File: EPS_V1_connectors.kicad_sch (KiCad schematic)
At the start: 4 parts, among them J1 Conn_01x20_Socket, J2 Conn_01x30_Socket, J3 Conn_01x15_Socket, J4 Conn_01x04_Socket

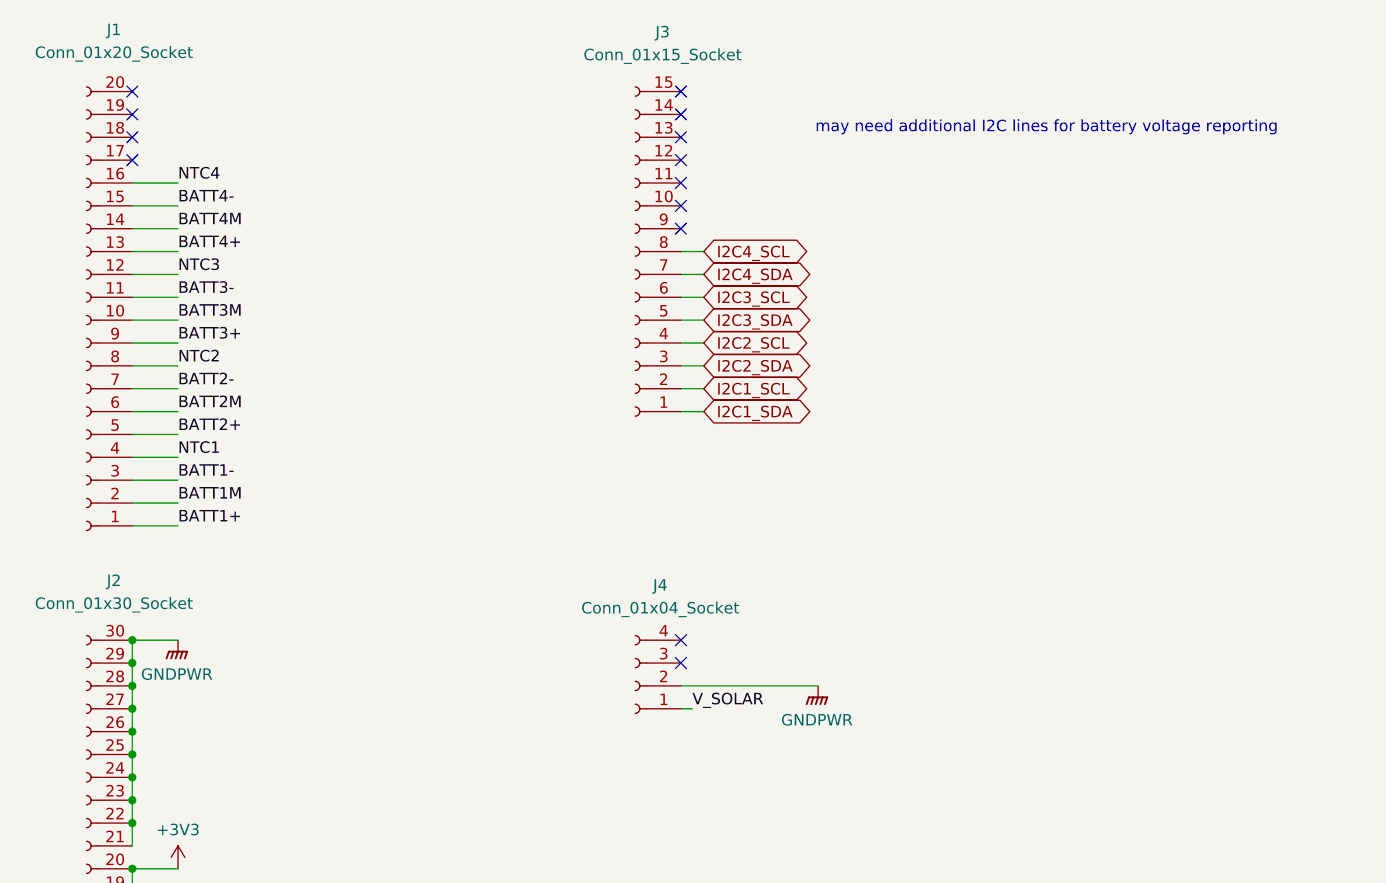
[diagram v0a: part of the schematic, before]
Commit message: Add fuel gauge, fix voltage labels
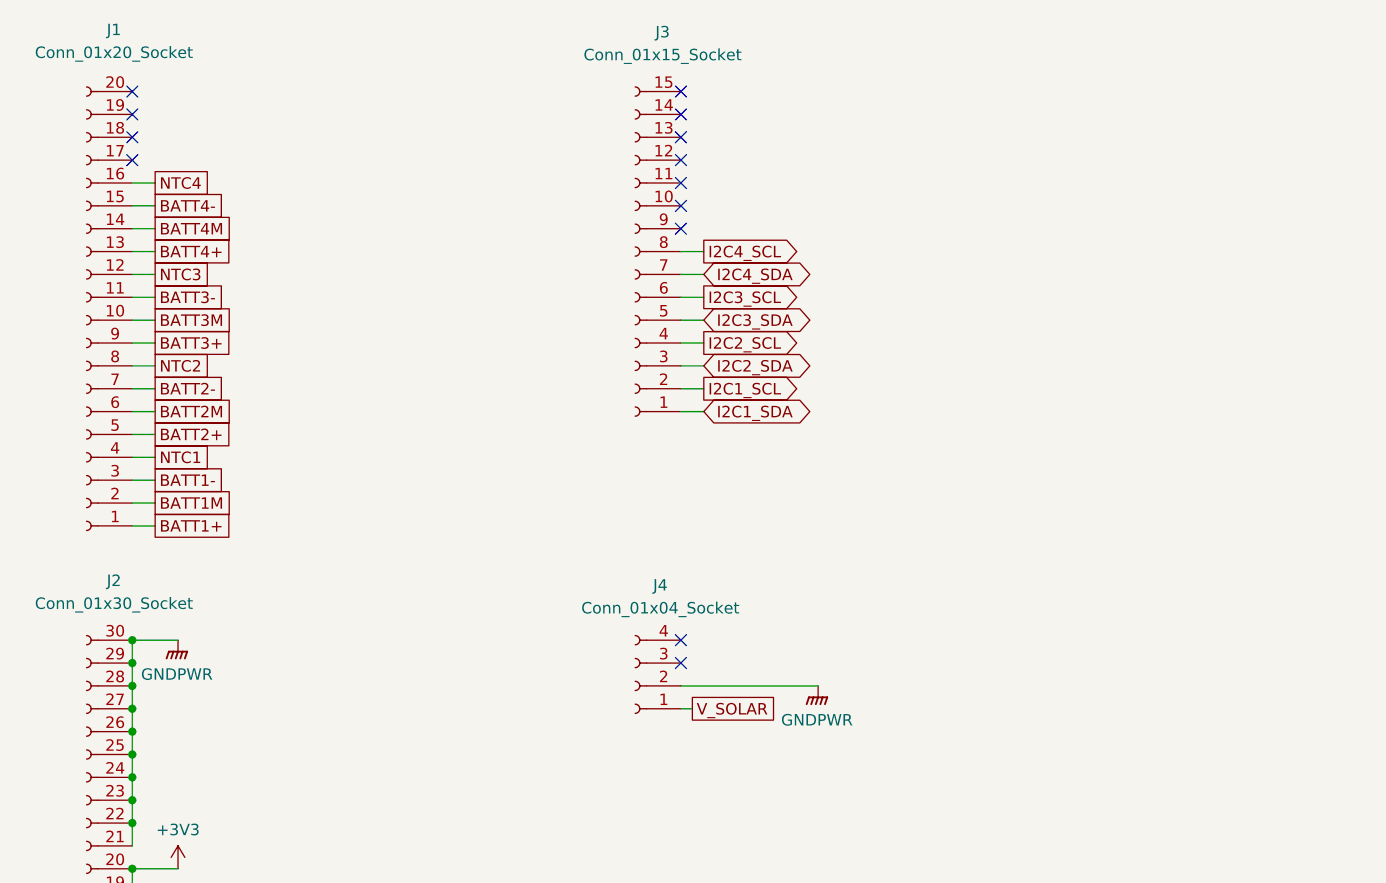
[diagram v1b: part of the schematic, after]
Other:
- note removed: "may need additional I2C lines for battery voltage reporting"

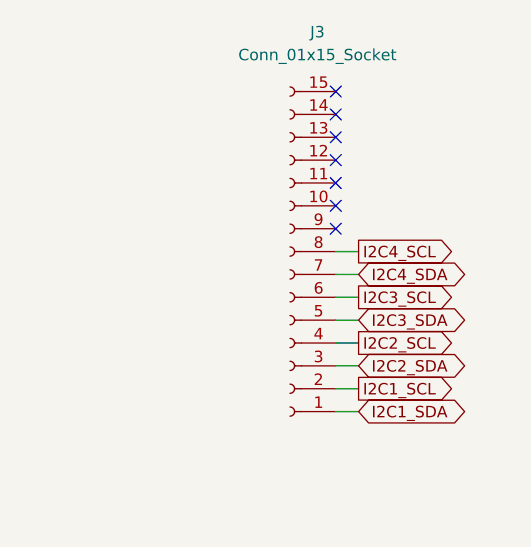
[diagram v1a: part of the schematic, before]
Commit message: Add fuel gauge ALRT lines
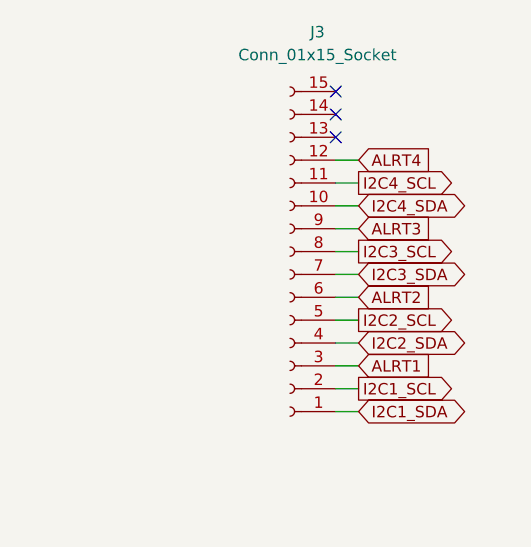
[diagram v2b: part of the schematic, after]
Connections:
- net I2C2_SCL: now also J3.5 (Pin_5); no longer J3.4 (Pin_4)
- net I2C2_SDA: now also J3.4 (Pin_4); no longer J3.3 (Pin_3)
- net I2C3_SCL: now also J3.8 (Pin_8); no longer J3.6 (Pin_6)
- net I2C3_SDA: now also J3.7 (Pin_7); no longer J3.5 (Pin_5)
- net I2C4_SCL: now also J3.11 (Pin_11); no longer J3.8 (Pin_8)
- net I2C4_SDA: now also J3.10 (Pin_10); no longer J3.7 (Pin_7)
- net ALRT4: now reaches J3.12 (Pin_12)
- net ALRT3: now reaches J3.9 (Pin_9)
- new net ALRT1: J3.3 (Pin_3)
- new net ALRT2: J3.6 (Pin_6)
- no-connect marks 13 -> 9

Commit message: Add boost converter to 12V, fix grounding
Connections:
- net +7V2 renamed +12V
- net GNDPWR renamed GND

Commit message: Add 12V boost values
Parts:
- added D1, D2, D3, D4: D_Schottky, symbol Device:D_Schottky
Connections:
- net V_SOLAR renamed VSOLAR
- new net VOUT: D1.1 (K), D2.1 (K), D3.1 (K), D4.1 (K)
- new net VOUT1: D1.2 (A)
- new net VOUT2: D2.2 (A)
- new net VOUT3: D3.2 (A)
- new net VOUT4: D4.2 (A)
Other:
- note added: "todo: add inhibit switch"
- note added: "todo: add inhibit switches"

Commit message: Add 5V charging input
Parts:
- added D5, D6: D_Schottky, symbol Device:D_Schottky
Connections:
- net GND: now also J1.18 (Pin_18)
- net VSOLAR: now also J1.17 (Pin_17); no longer J4.1 (Pin_1)
- new net VCHG: D6.2 (A), J4.1 (Pin_1)
- new net VIN: D5.1 (K), D6.1 (K)
- new net VSOLARR: D5.2 (A)
- no-connect marks 9 -> 7

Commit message: Clarify global net naming, other minor fixes
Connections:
- net VCHG renamed EXT_5V
- net VIN renamed CHG_IN
- net VOUT renamed CHG_OUT
- net VOUT1 renamed CHG_OUT1
- net VOUT2 renamed CHG_OUT2
- net VOUT3 renamed CHG_OUT3
- net VOUT4 renamed CHG_OUT4
- net VSOLAR renamed SOLAR
- net VSOLARR renamed SOLAR_5V
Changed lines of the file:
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@@
 	(wire
 		(pts
-			(xy 106.68 107.95) (xy 121.92 107.95)
+			(xy 106.68 107.95) (xy 119.38 107.95)
 		)
 		(stroke
@@
 		)
 	)
-	(global_label "VOUT2"
+	(global_label "CHG_OUT2"
 		(shape passive)
 		(at 194.31 71.12 180)
@@
 		)
 		(property "Intersheetrefs" "${INTERSHEET_REFS}"
-			(at 186.5094 71.12 0)
+			(at 182.7599 71.12 0)
 			(effects
 				(font
@@
 		)
 	)
-	(global_label "VIN"
+	(global_label "CHG_IN"
 		(shape passive)
 		(at 209.55 135.89 0)
@@
 		)
 		(property "Intersheetrefs" "${INTERSHEET_REFS}"
-			(at 214.4478 135.89 0)
+			(at 218.1973 135.89 0)
 			(effects
 				(font
@@
 		)
 	)
-	(global_label "VSOLARR"
+	(global_label "SOLAR_5V"
 		(shape passive)
 		(at 194.31 130.81 180)
@@
 		)
 		(property "Intersheetrefs" "${INTERSHEET_REFS}"
-			(at 184.1508 130.81 0)
+			(at 183.2437 130.81 0)
 			(effects
 				(font
@@
 		)
 	)
-	(global_label "VOUT3"
+	(global_label "CHG_OUT3"
 		(shape passive)
 		(at 194.31 81.28 180)
@@
 		)
 		(property "Intersheetrefs" "${INTERSHEET_REFS}"
-			(at 186.5094 81.28 0)
+			(at 182.7599 81.28 0)
 			(effects
 				(font
@@
 		)
 	)
-	(global_label "VCHG"
+	(global_label "EXT_5V"
 		(shape passive)
 		(at 106.68 110.49 0)
@@
 		)
 		(property "Intersheetrefs" "${INTERSHEET_REFS}"
-			(at 113.513 110.49 0)
-			(effects
-				(font
-					(size 1.27 1.27)
-				)
-				(justify left)
-				(hide yes)
-			)
-		)
-	)
-	(global_label "VSOLAR"
+			(at 115.1457 110.49 0)
+			(effects
+				(font
+					(size 1.27 1.27)
+				)
+				(justify left)
+				(hide yes)
+			)
+		)
+	)
+	(global_label "SOLAR"
 		(shape passive)
 		(at 48.26 49.53 0)
@@
 		)
 		(property "Intersheetrefs" "${INTERSHEET_REFS}"
-			(at 57.1492 49.53 0)
+			(at 56.0606 49.53 0)
 			(effects
 				(font
@@
 		)
 	)
-	(global_label "VOUT4"
+	(global_label "CHG_OUT4"
 		(shape passive)
 		(at 194.31 91.44 180)
@@
 		)
 		(property "Intersheetrefs" "${INTERSHEET_REFS}"
-			(at 186.5094 91.44 0)
+			(at 182.7599 91.44 0)
 			(effects
 				(font
@@
 		)
 	)
-	(global_label "VOUT1"
+	(global_label "CHG_OUT1"
 		(shape passive)
 		(at 194.31 60.96 180)
@@
 		)
 		(property "Intersheetrefs" "${INTERSHEET_REFS}"
-			(at 186.5094 60.96 0)
+			(at 182.7599 60.96 0)
 			(effects
 				(font
@@
 		)
 	)
-	(global_label "VCHG"
+	(global_label "EXT_5V"
 		(shape passive)
 		(at 194.31 140.97 180)
@@
 		)
 		(property "Intersheetrefs" "${INTERSHEET_REFS}"
-			(at 187.477 140.97 0)
+			(at 185.8443 140.97 0)
 			(effects
 				(font
@@
 		)
 	)
-	(global_label "VOUT"
+	(global_label "CHG_OUT"
 		(shape passive)
 		(at 243.84 76.2 0)
@@
 		)
 		(property "Intersheetrefs" "${INTERSHEET_REFS}"
-			(at 250.4311 76.2 0)
+			(at 254.1806 76.2 0)
 			(effects
 				(font
@@
 	(symbol
 		(lib_id "power:GND")
-		(at 121.92 107.95 0)
+		(at 119.38 107.95 0)
 		(unit 1)
 		(exclude_from_sim no)
@@
 		(dnp no)
 		(property "Reference" "#PWR034"
-			(at 121.92 114.3 0)
+			(at 119.38 114.3 0)
 			(effects
 				(font
@@
 		)
 		(property "Value" "GND"
-			(at 121.92 112.014 0)
+			(at 119.38 112.014 0)
 			(effects
 				(font
@@
 		)
 		(property "Footprint" ""
-			(at 121.92 107.95 0)
+			(at 119.38 107.95 0)
 			(effects
 				(font
@@
 		)
 		(property "Datasheet" ""
-			(at 121.92 107.95 0)
+			(at 119.38 107.95 0)
 			(effects
 				(font
@@
 		)
 		(property "Description" "Power symbol creates a global label with name \"GND\" , ground"
-			(at 121.92 107.95 0)
-			(effects
-				(font
+			(at 119.38 107.95 0)
+			(effects
+				(font

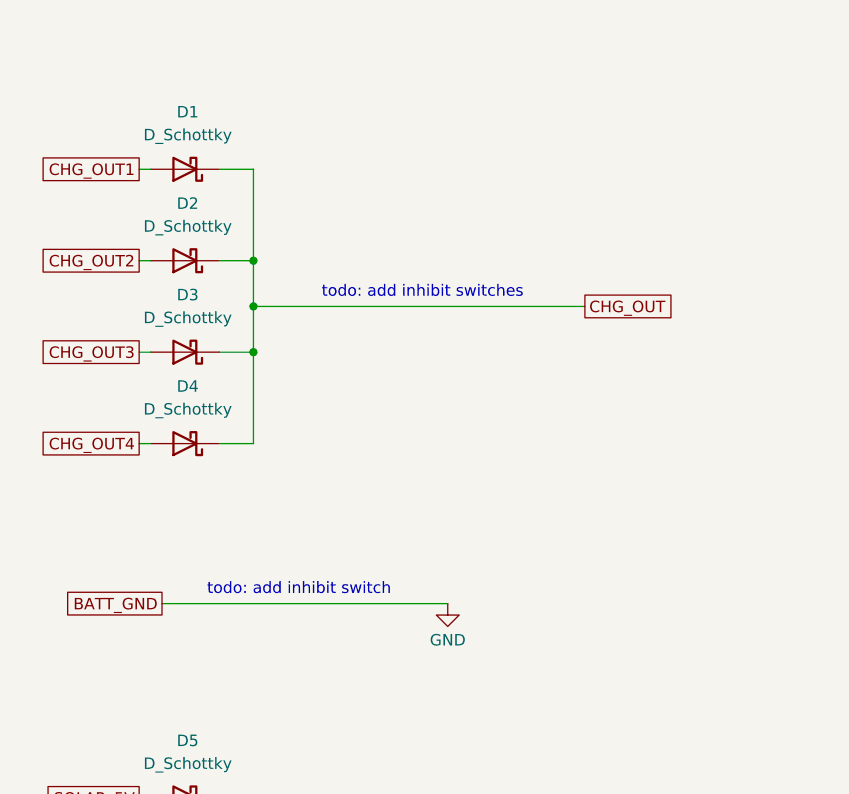
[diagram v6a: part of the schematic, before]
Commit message: Add inhibit switches
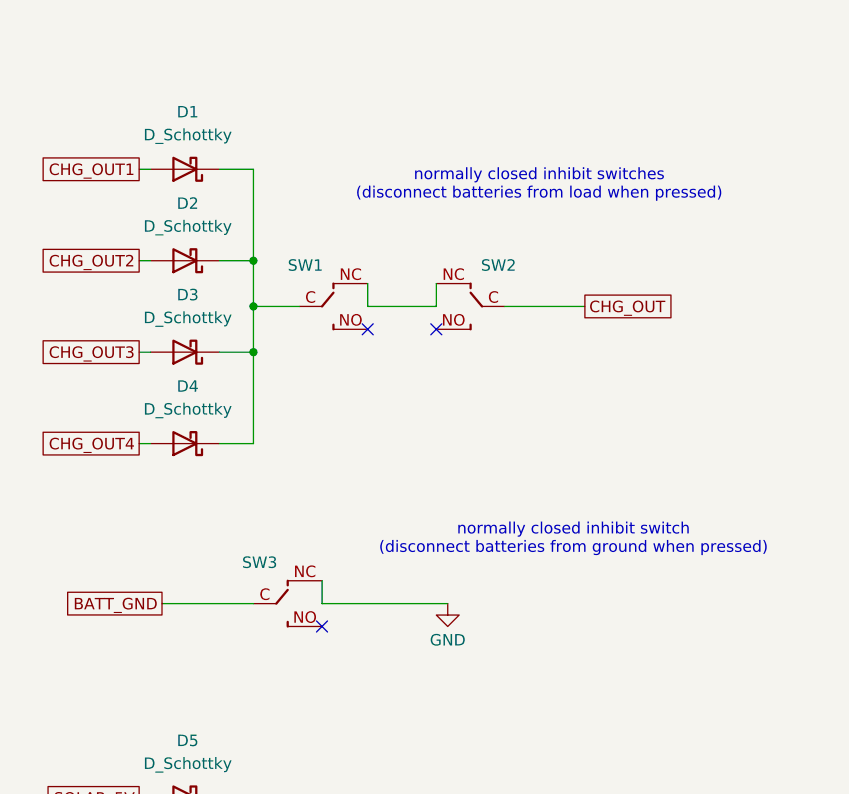
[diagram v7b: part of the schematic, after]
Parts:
- added SW1, SW3: OMRON D2F-L3-D (RIGHT), oresat-misc:D2F-L3-D-HORIZONTAL-R, symbol oresat-misc:OMRON-D2F-L3-D-RIGHT
- added SW2: OMRON D2F-L3-D (LEFT), oresat-misc:D2F-L3-D-HORIZONTAL-L, symbol oresat-misc:OMRON-D2F-L3-D-LEFT
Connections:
- net CHG_OUT: now also SW2.C (COM); no longer D1.1 (K), D2.1 (K), D3.1 (K), D4.1 (K)
- net GND: now also SW3.NC
- new net: D1.1 (K), D2.1 (K), D3.1 (K), D4.1 (K), SW1.C (COM)
- new net: SW1.NC, SW2.NC
- new net BATT_GND: SW3.C (COM)
- no-connect marks 7 -> 10
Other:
- note added: "normally closed inhibit switch (disconnect batteries from ground when pressed)"
- note added: "normally closed inhibit switches (disconnect batteries from load when pressed)"
- note removed: "todo: add inhibit switch"
- note removed: "todo: add inhibit switches"
